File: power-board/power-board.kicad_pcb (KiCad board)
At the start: 2 copper layers, 100 x 100 mm, 41 parts, among them P1 CONN_01X04, P10 CONN_01X04, P11 CONN_01X04, P12 CONN_01X04, P13 CONN_01X04, P14 CONN_01X04, P15 CONN_01X04, P16 CONN_01X04, P17 CONN_01X04, P18 CONN_01X04, P19 CONN_01X04, P2 CONN_01X04, P20 CONN_01X04, P21 CONN_01X04, P22 CONN_01X04, P23 CONN_01X04, P24 CONN_01X04, P25 CONN_01X04, P26 CONN_01X04, P27 CONN_01X04, P28 CONN_01X04, P29 CONN_01X04, P3 CONN_01X04, P30 CONN_01X04, P31 CONN_01X04, P32 CONN_01X04, P33 CONN_01X04, P34 CONN_01X04, P35 CONN_01X04, P36 CONN_01X04, P37 CONN_01X04, P38 CONN_01X04, P39 CONN_01X04, P4 CONN_01X04, P40 CONN_01X04, P41 CONN_01X04, P5 CONN_01X04, P6 CONN_01X04, P7 CONN_01X04, P8 CONN_01X04, P9 CONN_01X04

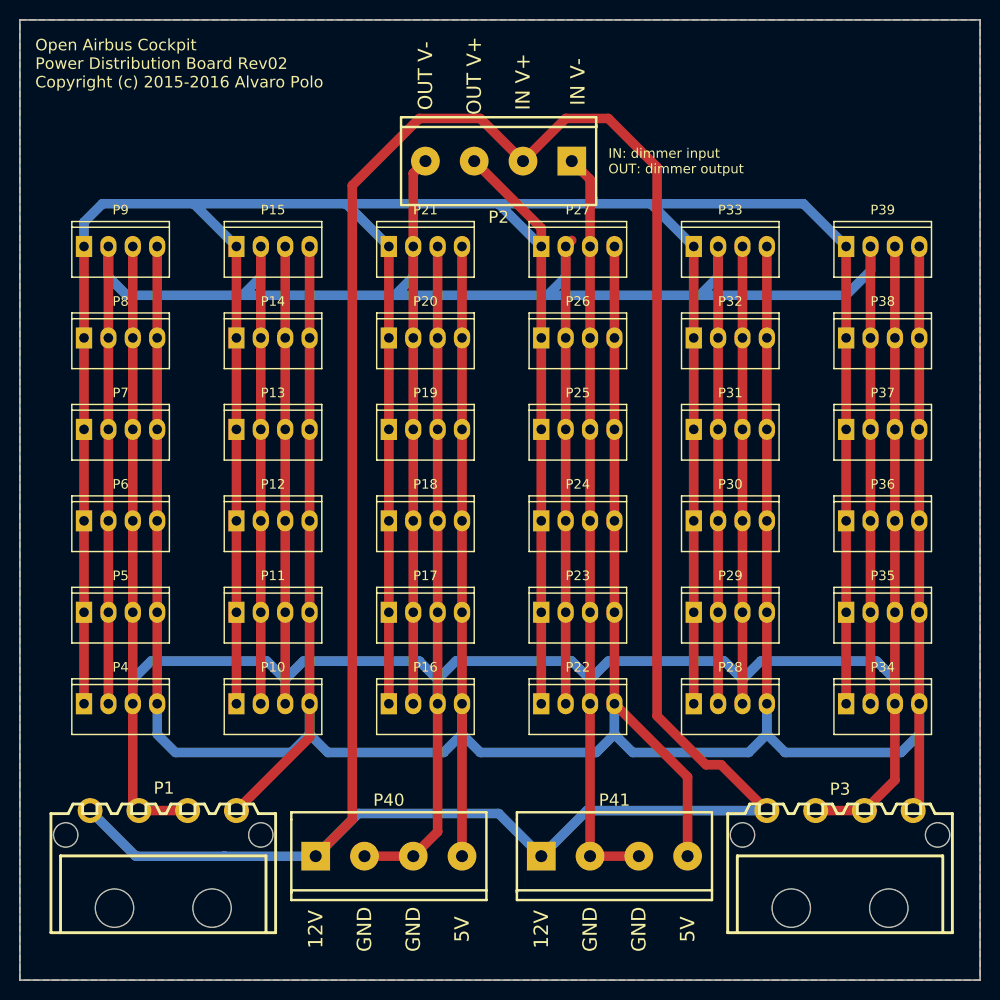
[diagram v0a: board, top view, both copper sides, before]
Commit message: Add M3 mounting holes to OAC Power Distrib board
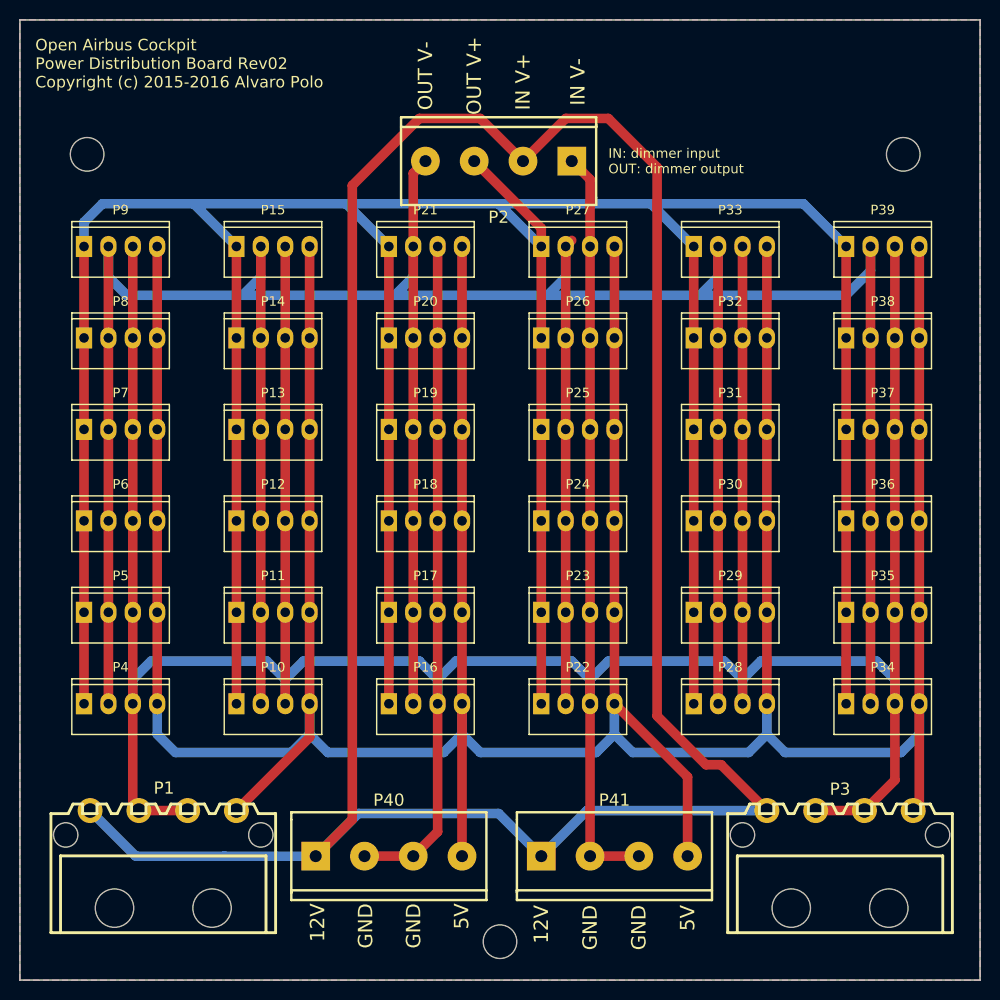
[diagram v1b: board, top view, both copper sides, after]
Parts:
- added REF**: MountingHole_3mm, Mounting_Holes:MountingHole_3-5mm, F.Cu at (152.0, 52.0)
- added REF**: MountingHole_3mm, Mounting_Holes:MountingHole_3-5mm, F.Cu at (67.0, 52.0)
- added REF**: MountingHole_3mm, Mounting_Holes:MountingHole_3-5mm, F.Cu at (110.0, 134.0)
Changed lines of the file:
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@@
     (tracks 236)
     (zones 0)
-    (modules 41)
+    (modules 44)
     (nets 6)
   )
@@
     )
   )
+  (module Mounting_Holes:MountingHole_3-5mm (layer F.Cu)
+    (at 152 52)
+    (descr "Mounting hole, Befestigungsbohrung, 3,5mm, No Annular, Kein Restring,")
+    (tags "Mounting hole, Befestigungsbohrung, 3,5mm, No Annular, Kein Restring,")
+    (fp_text reference REF** (at 0 -4.50088) (layer F.SilkS) hide
+      (effects (font (size 1 1) (thickness 0.15)))
+    )
+    (fp_text value MountingHole_3mm (at 0 5.00126) (layer F.Fab) hide
+      (effects (font (size 1 1) (thickness 0.15)))
+    )
+    (fp_circle (center 0 0) (end 3.5 0) (layer Cmts.User) (width 0.381))
+    (pad 1 thru_hole circle (at 0 0) (size 3.5 3.5) (drill 3.5) (layers))
+  )
+  (module Mounting_Holes:MountingHole_3-5mm (layer F.Cu)
+    (at 67 52)
+    (descr "Mounting hole, Befestigungsbohrung, 3,5mm, No Annular, Kein Restring,")
+    (tags "Mounting hole, Befestigungsbohrung, 3,5mm, No Annular, Kein Restring,")
+    (fp_text reference REF** (at 0 -4.50088) (layer F.SilkS) hide
+      (effects (font (size 1 1) (thickness 0.15)))
+    )
+    (fp_text value MountingHole_3mm (at 0 5.00126) (layer F.Fab) hide
+      (effects (font (size 1 1) (thickness 0.15)))
+    )
+    (fp_circle (center 0 0) (end 3.5 0) (layer Cmts.User) (width 0.381))
+    (pad 1 thru_hole circle (at 0 0) (size 3.5 3.5) (drill 3.5) (layers))
+  )
+  (module Mounting_Holes:MountingHole_3-5mm (layer F.Cu)
+    (at 110 134)
+    (descr "Mounting hole, Befestigungsbohrung, 3,5mm, No Annular, Kein Restring,")
+    (tags "Mounting hole, Befestigungsbohrung, 3,5mm, No Annular, Kein Restring,")
+    (fp_text reference REF** (at 0 -4.50088) (layer F.SilkS) hide
+      (effects (font (size 1 1) (thickness 0.15)))
+    )
+    (fp_text value MountingHole_3mm (at 0 5.00126) (layer F.Fab) hide
+      (effects (font (size 1 1) (thickness 0.15)))
+    )
+    (fp_circle (center 0 0) (end 3.5 0) (layer Cmts.User) (width 0.381))
+    (pad 1 thru_hole circle (at 0 0) (size 3.5 3.5) (drill 3.5) (layers))
+  )
   (gr_text "Open Airbus Cockpit\nPower Distribution Board Rev02\nCopyright (c) 2015-2016 Alvaro Polo\n" (at 61.595 42.545) (layer F.SilkS)
     (effects (font (size 1.2 1.2) (thickness 0.3)) (justify left))
@@
     (effects (font (size 1.5 1.5) (thickness 0.3)))
   )
-  (gr_text 5V (at 129.54 132.715 90) (layer F.SilkS)
-    (effects (font (size 1.5 1.5) (thickness 0.3)))
-  )
-  (gr_text GND (at 124.46 132.715 90) (layer F.SilkS)
-    (effects (font (size 1.5 1.5) (thickness 0.3)))
-  )
-  (gr_text GND (at 119.38 132.715 90) (layer F.SilkS)
-    (effects (font (size 1.5 1.5) (thickness 0.3)))
-  )
-  (gr_text 12V (at 114.3 132.715 90) (layer F.SilkS)
-    (effects (font (size 1.5 1.5) (thickness 0.3)))
-  )
-  (gr_text 5V (at 106.045 132.715 90) (layer F.SilkS)
-    (effects (font (size 1.5 1.5) (thickness 0.3)))
-  )
-  (gr_text GND (at 100.965 132.715 90) (layer F.SilkS)
-    (effects (font (size 1.5 1.5) (thickness 0.3)))
-  )
-  (gr_text GND (at 95.885 132.715 90) (layer F.SilkS)
-    (effects (font (size 1.5 1.5) (thickness 0.3)))
-  )
-  (gr_text 12V (at 90.805 132.715 90) (layer F.SilkS)
-    (effects (font (size 1.5 1.5) (thickness 0.3)))
+  (gr_text 5V (at 129.54 130.175 90) (layer F.SilkS)
+    (effects (font (size 1.5 1.5) (thickness 0.3)) (justify right))
+  )
+  (gr_text GND (at 124.46 130.175 90) (layer F.SilkS)
+    (effects (font (size 1.5 1.5) (thickness 0.3)) (justify right))
+  )
+  (gr_text GND (at 119.38 130.175 90) (layer F.SilkS)
+    (effects (font (size 1.5 1.5) (thickness 0.3)) (justify right))
+  )
+  (gr_text 12V (at 114.3 130.175 90) (layer F.SilkS)
+    (effects (font (size 1.5 1.5) (thickness 0.3)) (justify right))
+  )
+  (gr_text 5V (at 106 130 90) (layer F.SilkS)
+    (effects (font (size 1.5 1.5) (thickness 0.3)) (justify right))
+  )
+  (gr_text GND (at 101 130 90) (layer F.SilkS)
+    (effects (font (size 1.5 1.5) (thickness 0.3)) (justify right))
+  )
+  (gr_text GND (at 96 130 90) (layer F.SilkS)
+    (effects (font (size 1.5 1.5) (thickness 0.3)) (justify right))
+  )
+  (gr_text 12V (at 91 130 90) (layer F.SilkS)
+    (effects (font (size 1.5 1.5) (thickness 0.3)) (justify right))
   )
   (segment (start 112.395 52.705) (end 107.95 48.26) (width 1) (layer F.Cu) (net 1))
